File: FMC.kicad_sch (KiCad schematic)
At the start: 6 parts, among them P1 ASP-134604-01, P2 ASP-134604-01

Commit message: Fixed remaining ERC errors and Warnings
No changes affecting copper were made.
At the end of this commits changes all changes from this and the previous two commits were pulled into the PCB.
No changes to the layout occurred and no additional pcb error or warning were made

Detailed Changes:
-Saved the Local Symbol to the project symbol lib and relinked for
  - Q1 & Q2 (looks like symbol was removed from std lib)
  - Max4896 IC's (U14..U23)
  - U32 | ZXCT1009F
  - L8 | MDS1260
  - Q3
  - U33
  - U34 to include thermal pad definitions
  - Mounting holes (Caused a footprint linking error as we linked to a custom footprint)
  - L7 (Caused a footprint linking error as we linked to a custom footprint)
  - P1 & P2 FMC connectors

-Removed Footprint Filter on the following library symbols to clear the footprint linking error
  - DB37 Connectors
  - Relays
  - Mounting Holes
  - U36, U37, D4, L7, L8, U33

-Updated J5 from standard library (no visual change occurred)

-Added Power Flag directives to clear up some warning on various power rails.

-Excluded 5 remaining warnings with comments
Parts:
- H4, H5, H6, H7: symbol Mechanical:MountingHole_Pad -> AD7768_Digitizer_SLib:MountingHole_Pad
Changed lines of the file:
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@@
 	)
 	(symbol
-		(lib_id "Mechanical:MountingHole_Pad")
+		(lib_id "AD7768_Digitizer_SLib:MountingHole_Pad")
 		(at 365.125 31.115 0)
 		(unit 1)
@@
 	)
 	(symbol
-		(lib_id "Mechanical:MountingHole_Pad")
+		(lib_id "AD7768_Digitizer_SLib:MountingHole_Pad")
 		(at 365.125 20.32 0)
 		(unit 1)
@@
 	)
 	(symbol
-		(lib_id "Mechanical:MountingHole_Pad")
+		(lib_id "AD7768_Digitizer_SLib:MountingHole_Pad")
 		(at 338.455 20.32 0)
 		(unit 1)
@@
 	)
 	(symbol
-		(lib_id "Mechanical:MountingHole_Pad")
+		(lib_id "AD7768_Digitizer_SLib:MountingHole_Pad")
 		(at 338.455 31.115 0)
 		(unit 1)

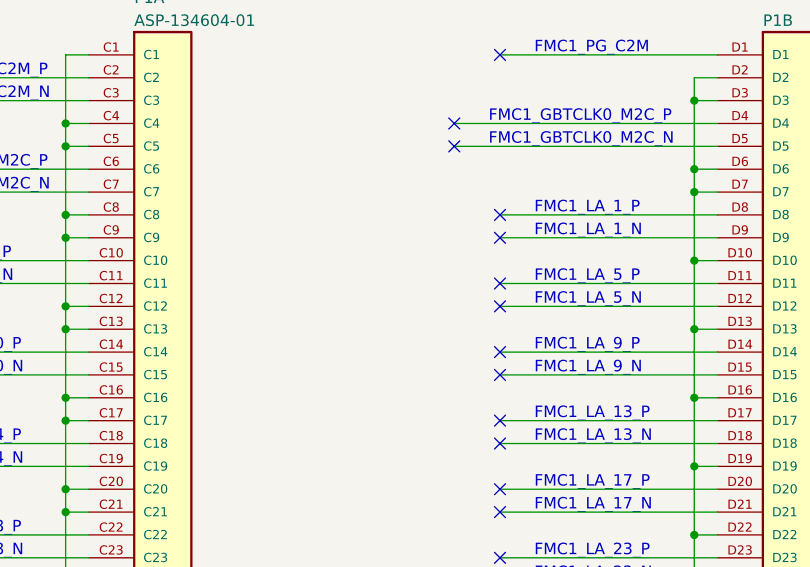
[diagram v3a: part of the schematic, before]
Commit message: Added Calibration EEPROM
-Added Calibration EEPROM
-Changed WP headers to 100mil spaced part
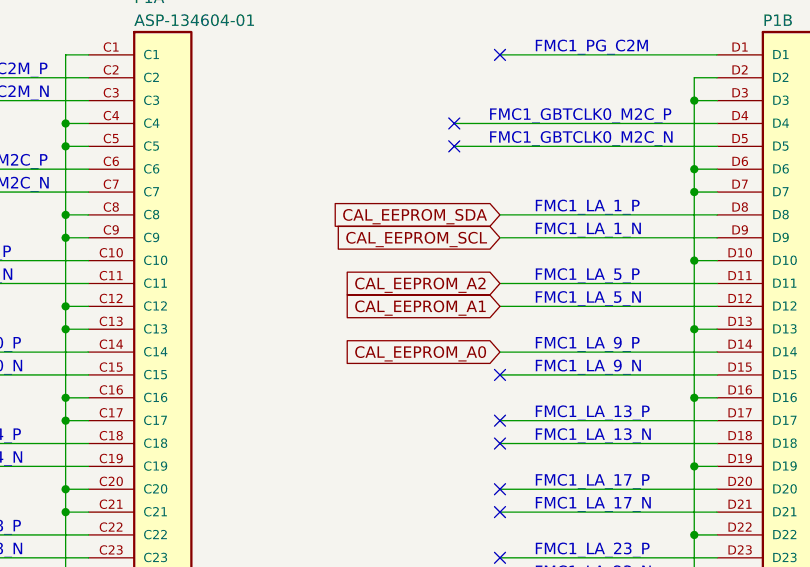
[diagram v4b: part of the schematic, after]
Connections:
- net CAL_EEPROM_A2: now reaches P1.D11
- net CAL_EEPROM_A1: now reaches P1.D12
- net CAL_EEPROM_A0: now reaches P1.D14
- net CAL_EEPROM_SDA: now reaches P1.D8
- net CAL_EEPROM_SCL: now reaches P1.D9
- no-connect marks 108 -> 103
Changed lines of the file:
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@@
 	)
 	(no_connect
-		(at 157.48 49.53)
-	)
-	(no_connect
 		(at 157.48 102.87)
 	)
@@
 	)
 	(no_connect
-		(at 157.48 39.37)
-	)
-	(no_connect
 		(at 226.06 24.13)
 	)
@@
 	)
 	(no_connect
-		(at 157.48 46.99)
-	)
-	(no_connect
 		(at 157.48 72.39)
 	)
@@
 	)
 	(no_connect
-		(at 157.48 57.15)
-	)
-	(no_connect
 		(at 87.63 186.69)
 	)
@@
 	)
 	(no_connect
-		(at 157.48 54.61)
+		(at 157.48 57.15)
 	)
 	(no_connect
@@
 	)
 	(no_connect
-		(at 157.48 41.91)
-	)
-	(no_connect
 		(at 226.06 57.15)
 	)
@@
 	(wire
 		(pts
+			(xy 157.48 49.53) (xy 181.61 49.53)
+		)
+		(stroke
+			(width 0)
+			(type default)
+		)
+	)
+	(wire
+		(pts
 			(xy 109.22 82.55) (xy 109.22 90.17)
 		)
@@
 	(wire
 		(pts
-			(xy 157.48 49.53) (xy 181.61 49.53)
-		)
-		(stroke
-			(width 0)
-			(type default)
-		)
-	)
-	(wire
-		(pts
 			(xy 293.37 151.13) (xy 317.5 151.13)
 		)
@@
 		)
 	)
+	(global_label "CAL_EEPROM_A0"
+		(shape input)
+		(at 157.48 54.61 180)
+		(fields_autoplaced yes)
+		(effects
+			(font
+				(size 1.27 1.27)
+			)
+			(justify right)
+		)
+		(property "Intersheetrefs" "${INTERSHEET_REFS}"
+			(at 139.2549 54.61 0)
+			(effects
+				(font
+					(size 1.27 1.27)
+				)
+				(justify right)
+				(hide yes)
+			)
+		)
+	)
 	(global_label "P2_Timing_Input"
 		(shape output)
@@
 		)
 	)
+	(global_label "CAL_EEPROM_A1"
+		(shape input)
+		(at 157.48 49.53 180)
+		(fields_autoplaced yes)
+		(effects
+			(font
+				(size 1.27 1.27)
+			)
+			(justify right)
+		)
+		(property "Intersheetrefs" "${INTERSHEET_REFS}"
+			(at 139.2549 49.53 0)
+			(effects
+				(font
+					(size 1.27 1.27)
+				)
+				(justify right)
+				(hide yes)
+			)
+		)
+	)
 	(global_label "ADC3_DO2"
 		(shape input)
@@
 		)
 	)
+	(global_label "CAL_EEPROM_A2"
+		(shape input)
+		(at 157.48 46.99 180)
+		(fields_autoplaced yes)
+		(effects
+			(font
+				(size 1.27 1.27)
+			)
+			(justify right)
+		)
+		(property "Intersheetrefs" "${INTERSHEET_REFS}"
+			(at 139.2549 46.99 0)
+			(effects
+				(font
+					(size 1.27 1.27)
+				)
+				(justify right)
+				(hide yes)
+			)
+		)
+	)
 	(global_label "ADC4_~{DRDY}"
 		(shape input)
@@
 		)
 	)
+	(global_label "CAL_EEPROM_SDA"
+		(shape input)
+		(at 157.48 39.37 180)
+		(fields_autoplaced yes)
+		(effects
+			(font
+				(size 1.27 1.27)
+			)
+			(justify right)
+		)
+		(property "Intersheetrefs" "${INTERSHEET_REFS}"
+			(at 137.9849 39.37 0)
+			(effects
+				(font
+					(size 1.27 1.27)
+				)
+				(justify right)
+				(hide yes)
+			)
+		)
+	)
 	(global_label "P2_ValidCLK"
 		(shape input)
@@
 			(effects
 				(font
+					(size 1.27 1.27)
+				)
+				(justify right)
+				(hide yes)
+			)
+		)
+	)
+	(global_label "CAL_EEPROM_SCL"
+		(shape input)
+		(at 157.48 41.91 180)
+		(fields_autoplaced yes)
+		(effects
+			(font
+				(size 1.27 1.27)
+			)
+			(justify right)
+		)
+		(property "Intersheetrefs" "${INTERSHEET_REFS}"
+			(at 138.0454 41.91 0)
+			(effects
+				(font

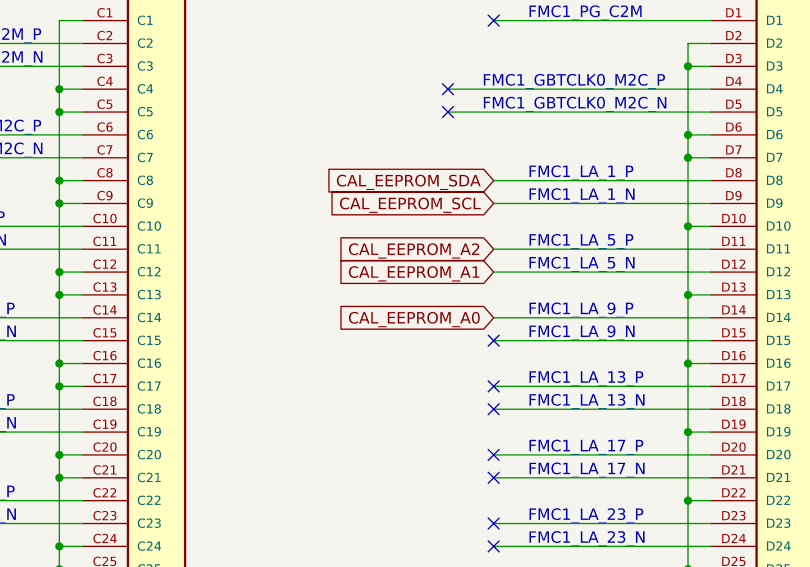
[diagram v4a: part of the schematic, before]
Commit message: Changed Cal EEPROM to run off 2.5V
Changed Cal EEPROM to run off 2.5V
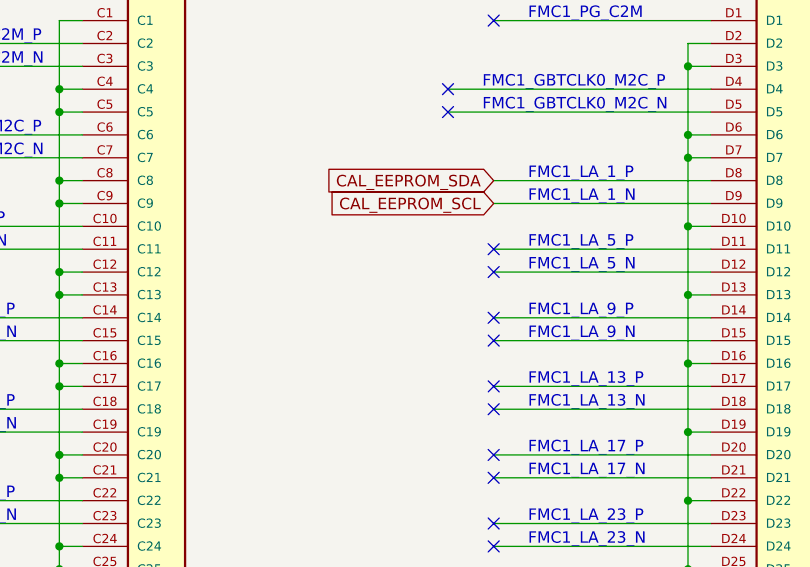
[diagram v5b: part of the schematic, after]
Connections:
- net CAL_EEPROM_A0: no longer names the net of P1.D14
- net CAL_EEPROM_A1: no longer names the net of P1.D12
- net CAL_EEPROM_A2: no longer names the net of P1.D11
- no-connect marks 103 -> 106
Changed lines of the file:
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@@
 	)
 	(no_connect
+		(at 157.48 54.61)
+	)
+	(no_connect
 		(at 226.06 49.53)
 	)
@@
 	)
 	(no_connect
+		(at 157.48 46.99)
+	)
+	(no_connect
 		(at 87.63 146.05)
 	)
@@
 	)
 	(no_connect
+		(at 157.48 49.53)
+	)
+	(no_connect
 		(at 87.63 166.37)
 	)
@@
 		)
 	)
-	(global_label "CAL_EEPROM_A0"
-		(shape input)
-		(at 157.48 54.61 180)
-		(fields_autoplaced yes)
-		(effects
-			(font
-				(size 1.27 1.27)
-			)
-			(justify right)
-		)
-		(property "Intersheetrefs" "${INTERSHEET_REFS}"
-			(at 139.2549 54.61 0)
-			(effects
-				(font
-					(size 1.27 1.27)
-				)
-				(justify right)
-				(hide yes)
-			)
-		)
-	)
 	(global_label "P2_Timing_Input"
 		(shape output)
@@
 		)
 	)
-	(global_label "CAL_EEPROM_A1"
-		(shape input)
-		(at 157.48 49.53 180)
-		(fields_autoplaced yes)
-		(effects
-			(font
-				(size 1.27 1.27)
-			)
-			(justify right)
-		)
-		(property "Intersheetrefs" "${INTERSHEET_REFS}"
-			(at 139.2549 49.53 0)
-			(effects
-				(font
-					(size 1.27 1.27)
-				)
-				(justify right)
-				(hide yes)
-			)
-		)
-	)
 	(global_label "ADC3_DO2"
 		(shape input)
@@
 			(effects
 				(font
-					(size 1.27 1.27)
-				)
-				(justify right)
-				(hide yes)
-			)
-		)
-	)
-	(global_label "CAL_EEPROM_A2"
-		(shape input)
-		(at 157.48 46.99 180)
-		(fields_autoplaced yes)
-		(effects
-			(font
-				(size 1.27 1.27)
-			)
-			(justify right)
-		)
-		(property "Intersheetrefs" "${INTERSHEET_REFS}"
-			(at 139.2549 46.99 0)
-			(effects
-				(font
